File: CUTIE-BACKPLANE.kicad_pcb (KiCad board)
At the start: 2 copper layers, 6 parts, among them J1 ERF8-025-05.0-L-DV-L-K-TR, J2 ERF8-025-05.0-L-DV-L-K-TR, J3 ERF8-025-05.0-L-DV-L-K-TR, J4 ERF8-025-05.0-L-DV-L-K-TR, J5 ERF8-025-05.0-L-DV-L-K-TR, J6 ERF8-025-05.0-L-DV-L-K-TR

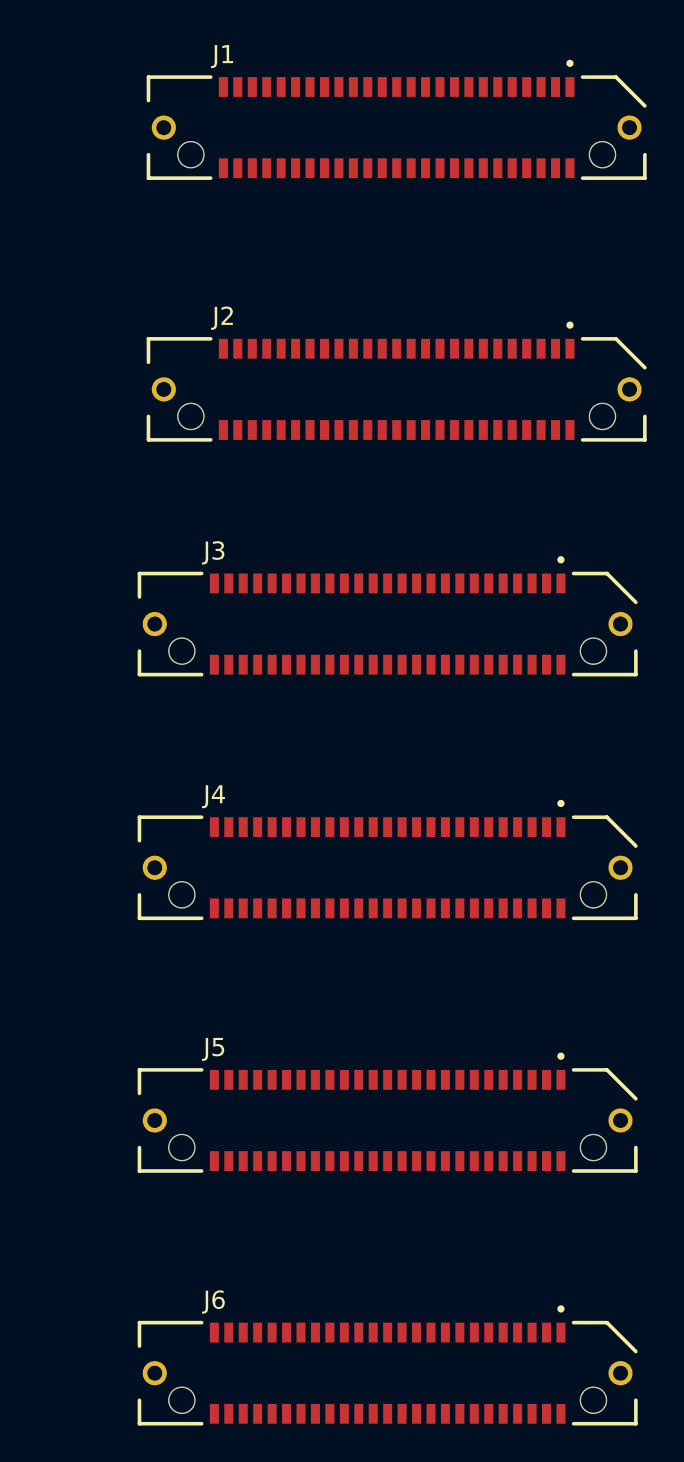
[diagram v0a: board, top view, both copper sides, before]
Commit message: fixed footprint link
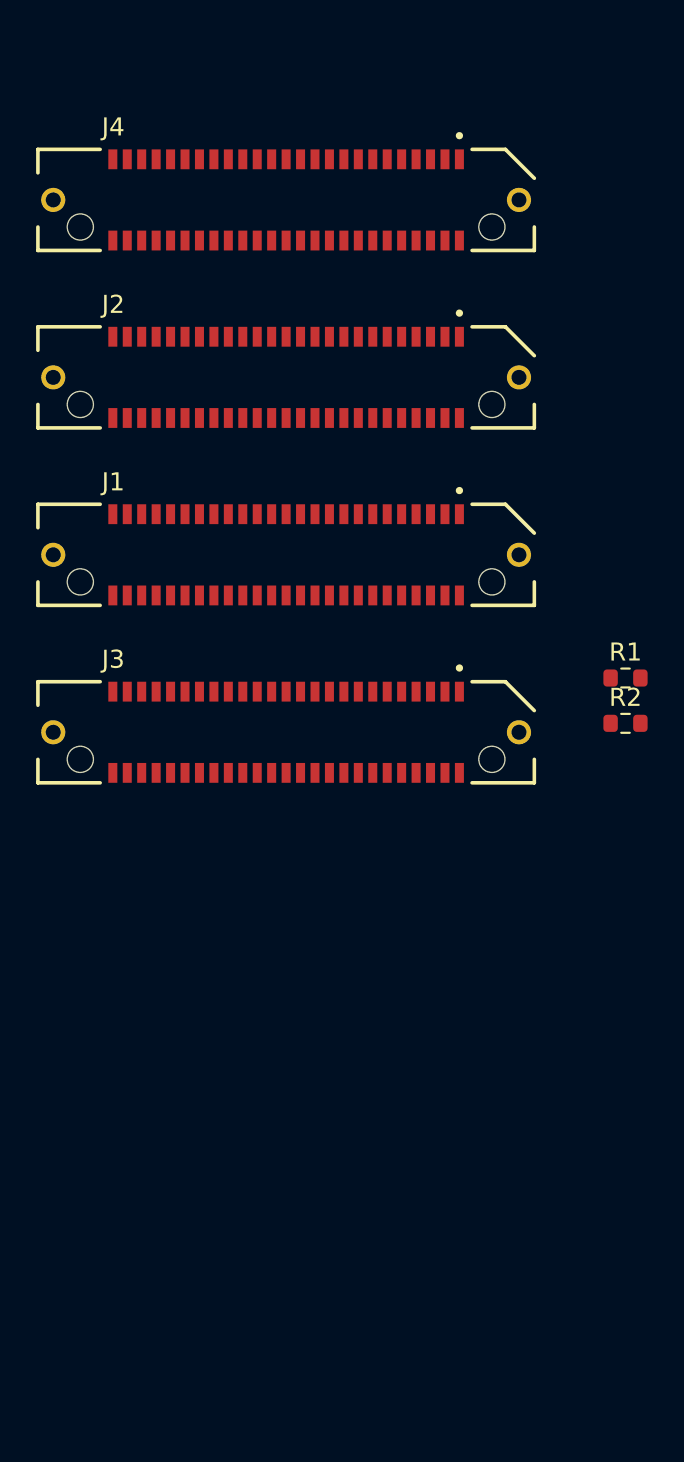
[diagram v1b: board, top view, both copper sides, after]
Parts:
- removed J5, J6: ERF8-025-05.0-L-DV-L-K-TR, library:SAMTEC_ERF8-025-05.0-L-DV-L-K-TR
- added R1: 120, Resistor_SMD:R_0603_1608Metric, F.Cu at (163.2, 95.0)
- added R2: 120, Resistor_SMD:R_0603_1608Metric, F.Cu at (163.2, 97.5)
- moved J4 37.4 mm to (144.4, 68.5)
- moved J1 24.4 mm to (144.4, 88.2)
- moved J3 8.22 mm to (144.4, 98.0)
- moved J2 6.16 mm to (144.4, 78.3)
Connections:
- J1 pad 01: (no net) -> /Slot 1/CAN0.L
- J1 pad 02: (no net) -> GND
- J1 pad 03: (no net) -> /Slot 1/CAN0.H
- J1 pad 04: (no net) -> GND
- J1 pad 05: (no net) -> GND
- J1 pad 06: (no net) -> unconnected-(J1-Pad06)
- J1 pad 07: (no net) -> GND
- J1 pad 08: (no net) -> unconnected-(J1-Pad08)
- J1 pad 09: (no net) -> unconnected-(J1-Pad09)
- J1 pad 10: unconnected-(J1-Pad10) -> GND
- J1 pad 12: unconnected-(J1-Pad12) -> GND
- J1 pad 13: unconnected-(J1-Pad13) -> GND
- J1 pad 15: unconnected-(J1-Pad15) -> GND
- J1 pad 18: unconnected-(J1-Pad18) -> GND
- J1 pad 20: unconnected-(J1-Pad20) -> GND
- J1 pad 21: unconnected-(J1-Pad21) -> GND
- J1 pad 22: unconnected-(J1-Pad22) -> GND
- J1 pad 23: unconnected-(J1-Pad23) -> GND
- J1 pad 24: unconnected-(J1-Pad24) -> GND
- J1 pad 25: unconnected-(J1-Pad25) -> GND
- J1 pad 26: unconnected-(J1-Pad26) -> GND
- J1 pad 27: unconnected-(J1-Pad27) -> GND
- J1 pad 28: unconnected-(J1-Pad28) -> GND
- J1 pad 29: unconnected-(J1-Pad29) -> GND
- J1 pad 30: unconnected-(J1-Pad30) -> GND
- J1 pad 31: unconnected-(J1-Pad31) -> /Slot 1/5V0_3
- J1 pad 32: unconnected-(J1-Pad32) -> /Slot 1/5V0_USB
- J1 pad 33: unconnected-(J1-Pad33) -> /Slot 1/5V0_3
- J1 pad 34: unconnected-(J1-Pad34) -> /Slot 1/5V0_USB
- J1 pad 35: unconnected-(J1-Pad35) -> /Slot 1/5V0_3
- J1 pad 36: unconnected-(J1-Pad36) -> /Slot 1/5V0_USB
- J1 pad 37: unconnected-(J1-Pad37) -> /Slot 1/5V0_3
- J1 pad 38: unconnected-(J1-Pad38) -> /Slot 1/5V0_USB
- J1 pad 39: unconnected-(J1-Pad39) -> /Slot 1/5V0_3
- J1 pad 40: unconnected-(J1-Pad40) -> /Slot 1/5V0_USB
- J1 pad 41: unconnected-(J1-Pad41) -> /Slot 1/5V0_1
- J1 pad 42: unconnected-(J1-Pad42) -> /Slot 1/5V0_2
- J1 pad 43: unconnected-(J1-Pad43) -> /Slot 1/5V0_1
- J1 pad 44: unconnected-(J1-Pad44) -> /Slot 1/5V0_2
- J1 pad 45: unconnected-(J1-Pad45) -> /Slot 1/5V0_1
- J1 pad 46: unconnected-(J1-Pad46) -> /Slot 1/5V0_2
- J1 pad 47: unconnected-(J1-Pad47) -> /Slot 1/5V0_1
- J1 pad 48: unconnected-(J1-Pad48) -> /Slot 1/5V0_2
- J1 pad 49: unconnected-(J1-Pad49) -> /Slot 1/5V0_1
- J1 pad 50: unconnected-(J1-Pad50) -> /Slot 1/5V0_2
- J2 pad 01: (no net) -> /Slot 1/CAN0.L
- J2 pad 02: (no net) -> GND
- J2 pad 03: (no net) -> /Slot 1/CAN0.H
- J2 pad 04: (no net) -> GND
- J2 pad 05: (no net) -> GND
- J2 pad 06: (no net) -> /Slot 2/USB3.D_N
- J2 pad 07: (no net) -> GND
- J2 pad 08: (no net) -> /Slot 2/USB3.D_P
- J2 pad 09: (no net) -> unconnected-(J2-Pad09)
- J2 pad 10: unconnected-(J2-Pad10) -> GND
- J2 pad 12: unconnected-(J2-Pad12) -> GND
- J2 pad 13: unconnected-(J2-Pad13) -> GND
- J2 pad 14: unconnected-(J2-Pad14) -> /Slot 2/USB3.RX_N
- J2 pad 15: unconnected-(J2-Pad15) -> GND
- J2 pad 16: unconnected-(J2-Pad16) -> /Slot 2/USB3.RX_P
- J2 pad 18: unconnected-(J2-Pad18) -> GND
- J2 pad 20: unconnected-(J2-Pad20) -> GND
- J2 pad 21: unconnected-(J2-Pad21) -> GND
- J2 pad 22: unconnected-(J2-Pad22) -> /Slot 2/USB3.TX_N
- J2 pad 23: unconnected-(J2-Pad23) -> GND
- J2 pad 24: unconnected-(J2-Pad24) -> /Slot 2/USB3.TX_P
- J2 pad 26: unconnected-(J2-Pad26) -> GND
- J2 pad 28: unconnected-(J2-Pad28) -> GND
- J2 pad 29: unconnected-(J2-Pad29) -> GND
- J2 pad 30: unconnected-(J2-Pad30) -> /Slot 2/CMRF.MOSI
- J2 pad 31: unconnected-(J2-Pad31) -> GND
- J2 pad 32: unconnected-(J2-Pad32) -> /Slot 2/CMRF.MISO
- J2 pad 34: unconnected-(J2-Pad34) -> GND
- J2 pad 36: unconnected-(J2-Pad36) -> GND
- J2 pad 37: unconnected-(J2-Pad37) -> GND
- J2 pad 38: unconnected-(J2-Pad38) -> /Slot 2/CMRF.SCLK
- J2 pad 39: unconnected-(J2-Pad39) -> GND
- J2 pad 40: unconnected-(J2-Pad40) -> /Slot 2/CMRF.CS0n
- J2 pad 41: unconnected-(J2-Pad41) -> /Slot 1/5V0_1
- J2 pad 42: unconnected-(J2-Pad42) -> GND
- J2 pad 43: unconnected-(J2-Pad43) -> /Slot 1/5V0_1
- J2 pad 44: unconnected-(J2-Pad44) -> GND
- J2 pad 45: unconnected-(J2-Pad45) -> /Slot 1/5V0_1
- J2 pad 47: unconnected-(J2-Pad47) -> /Slot 1/5V0_1
- J2 pad 49: unconnected-(J2-Pad49) -> /Slot 1/5V0_1
- J2 pad 50: unconnected-(J2-Pad50) -> GND
- J3 pad 01: (no net) -> /Slot 1/CAN0.L
- J3 pad 02: (no net) -> GND
- J3 pad 03: (no net) -> /Slot 1/CAN0.H
- J3 pad 04: (no net) -> GND
- J3 pad 05: (no net) -> GND
- J3 pad 06: (no net) -> unconnected-(J3-Pad06)
- J3 pad 07: (no net) -> GND
- J3 pad 08: (no net) -> unconnected-(J3-Pad08)
- J3 pad 09: (no net) -> unconnected-(J3-Pad09)
- J3 pad 10: unconnected-(J3-Pad10) -> GND
- J3 pad 12: unconnected-(J3-Pad12) -> GND
- J3 pad 13: unconnected-(J3-Pad13) -> GND
- J3 pad 15: unconnected-(J3-Pad15) -> GND
- J3 pad 18: unconnected-(J3-Pad18) -> GND
- J3 pad 20: unconnected-(J3-Pad20) -> GND
- J3 pad 21: unconnected-(J3-Pad21) -> GND
- J3 pad 23: unconnected-(J3-Pad23) -> GND
- J3 pad 26: unconnected-(J3-Pad26) -> GND
- J3 pad 28: unconnected-(J3-Pad28) -> GND
- J3 pad 29: unconnected-(J3-Pad29) -> GND
- J3 pad 31: unconnected-(J3-Pad31) -> GND
- J3 pad 34: unconnected-(J3-Pad34) -> GND
- J3 pad 36: unconnected-(J3-Pad36) -> GND
- J3 pad 37: unconnected-(J3-Pad37) -> GND
- J3 pad 39: unconnected-(J3-Pad39) -> GND
- J3 pad 41: unconnected-(J3-Pad41) -> /Slot 1/5V0_2
- J3 pad 42: unconnected-(J3-Pad42) -> GND
- J3 pad 43: unconnected-(J3-Pad43) -> /Slot 1/5V0_2
- J3 pad 44: unconnected-(J3-Pad44) -> GND
- J3 pad 45: unconnected-(J3-Pad45) -> /Slot 1/5V0_2
- J3 pad 47: unconnected-(J3-Pad47) -> /Slot 1/5V0_2
- J3 pad 49: unconnected-(J3-Pad49) -> /Slot 1/5V0_2
- J3 pad 50: unconnected-(J3-Pad50) -> GND
- J4 pad 01: (no net) -> /Slot 1/CAN0.L
- J4 pad 02: (no net) -> GND
- J4 pad 03: (no net) -> /Slot 1/CAN0.H
- J4 pad 04: (no net) -> GND
- J4 pad 05: (no net) -> GND
- J4 pad 06: (no net) -> unconnected-(J4-Pad06)
- J4 pad 07: (no net) -> GND
- J4 pad 08: (no net) -> unconnected-(J4-Pad08)
- J4 pad 09: (no net) -> unconnected-(J4-Pad09)
- J4 pad 10: unconnected-(J4-Pad10) -> GND
- J4 pad 12: unconnected-(J4-Pad12) -> GND
- J4 pad 13: unconnected-(J4-Pad13) -> GND
- J4 pad 15: unconnected-(J4-Pad15) -> GND
- J4 pad 18: unconnected-(J4-Pad18) -> GND
- J4 pad 20: unconnected-(J4-Pad20) -> GND
- J4 pad 21: unconnected-(J4-Pad21) -> GND
- J4 pad 23: unconnected-(J4-Pad23) -> GND
- J4 pad 26: unconnected-(J4-Pad26) -> GND
- J4 pad 28: unconnected-(J4-Pad28) -> GND
- J4 pad 29: unconnected-(J4-Pad29) -> GND
- J4 pad 30: unconnected-(J4-Pad30) -> /Slot 2/CMRF.MOSI
- J4 pad 31: unconnected-(J4-Pad31) -> GND
- J4 pad 32: unconnected-(J4-Pad32) -> /Slot 2/CMRF.MISO
- J4 pad 34: unconnected-(J4-Pad34) -> GND
- J4 pad 36: unconnected-(J4-Pad36) -> GND
- J4 pad 37: unconnected-(J4-Pad37) -> GND
- J4 pad 38: unconnected-(J4-Pad38) -> /Slot 2/CMRF.SCLK
- J4 pad 39: unconnected-(J4-Pad39) -> GND
- J4 pad 40: unconnected-(J4-Pad40) -> /Slot 2/CMRF.CS0n
- J4 pad 41: unconnected-(J4-Pad41) -> /Slot 1/5V0_3
- J4 pad 42: unconnected-(J4-Pad42) -> GND
- J4 pad 43: unconnected-(J4-Pad43) -> /Slot 1/5V0_3
- J4 pad 44: unconnected-(J4-Pad44) -> GND
- J4 pad 45: unconnected-(J4-Pad45) -> /Slot 1/5V0_3
- J4 pad 47: unconnected-(J4-Pad47) -> /Slot 1/5V0_3
- J4 pad 49: unconnected-(J4-Pad49) -> /Slot 1/5V0_3
- J4 pad 50: unconnected-(J4-Pad50) -> GND

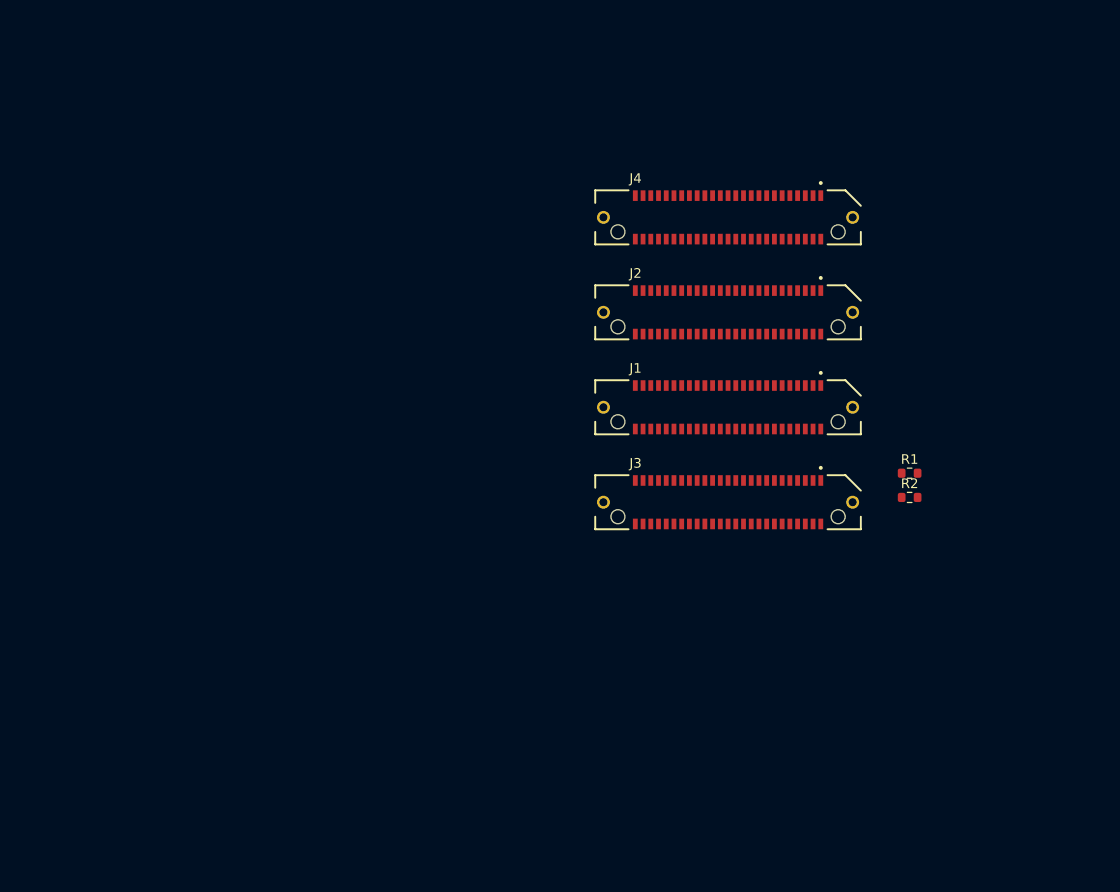
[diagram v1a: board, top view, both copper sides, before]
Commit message: added pwr leds and edge cuts
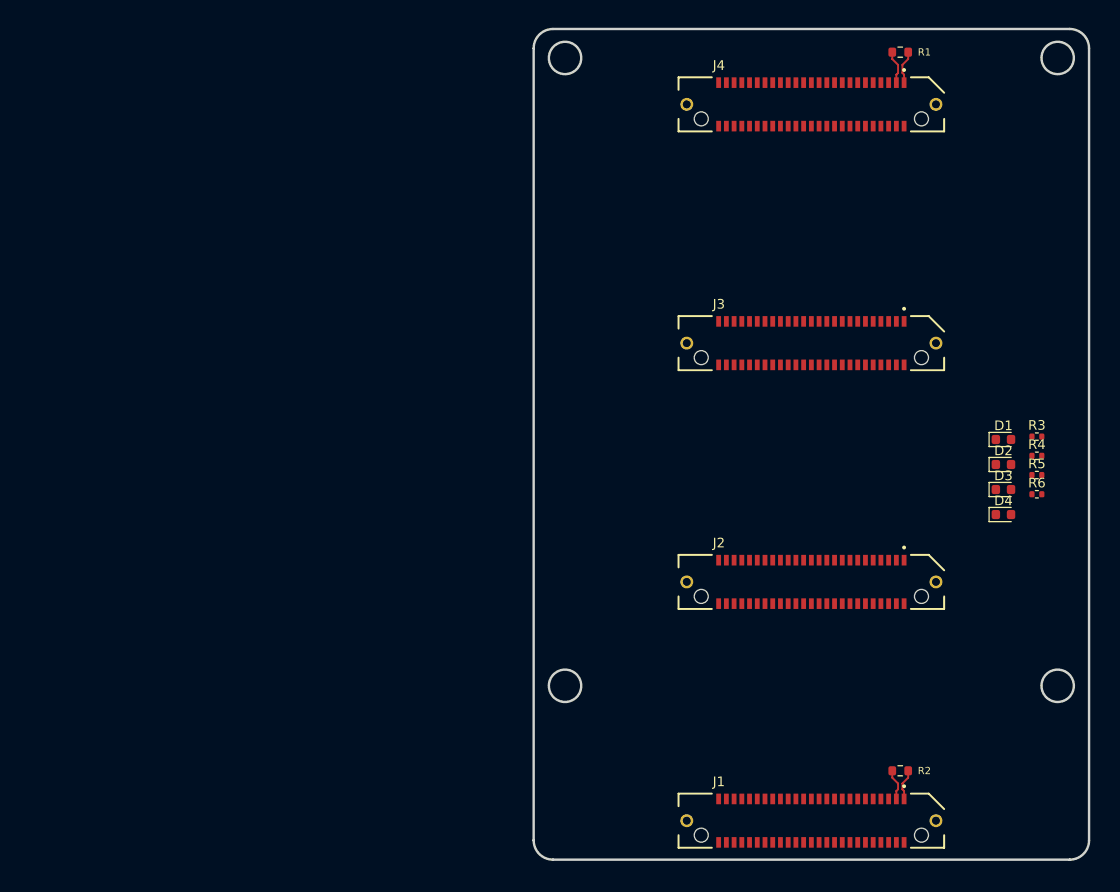
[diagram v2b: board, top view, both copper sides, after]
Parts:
- added D1: LED Red, LED_SMD:LED_0603_1608Metric, F.Cu at (172.9, 91.5)
- added D2: LED Red, LED_SMD:LED_0603_1608Metric, F.Cu at (172.9, 94.1)
- added D3: LED Red, LED_SMD:LED_0603_1608Metric, F.Cu at (172.9, 96.7)
- added D4: LED Red, LED_SMD:LED_0603_1608Metric, F.Cu at (172.9, 99.3)
- added R3: 1k, Resistor_SMD:R_0402_1005Metric, F.Cu at (176.3, 91.2)
- added R4: 1k, Resistor_SMD:R_0402_1005Metric, F.Cu at (176.3, 93.2)
- added R5: 1k, Resistor_SMD:R_0402_1005Metric, F.Cu at (176.3, 95.2)
- added R6: 1k, Resistor_SMD:R_0402_1005Metric, F.Cu at (176.3, 97.2)
- moved J1 43.7 mm to (153.0, 131.0)
- moved R1 43.6 mm to (162.2, 51.4)
- moved J2 29.2 mm to (153.0, 106.2)
- moved R2 28.3 mm to (162.2, 125.8)
- moved J3 18.6 mm to (153.0, 81.5)
- moved J4 14.5 mm to (153.0, 56.8)
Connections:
- net /Slot 1/CAN0.H renamed /Slot 1/CAN0.P
- net /Slot 1/CAN0.L renamed /Slot 1/CAN0.N
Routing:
- net /Slot 1/CAN0.P: track 0.00 -> 6.71 mm
- net /Slot 1/CAN0.N: track 0.00 -> 6.71 mm
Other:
- board outline added: 57.5 x 86 mm

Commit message: prelim layout complete
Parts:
- added J7: USB3_A, library:CONN9_08-0003_MOL, F.Cu at (156.0, 94.0)
- moved R5 57.1 mm to (134.8, 56.0)
- moved D3 56.8 mm to (134.8, 54.5)
- moved R3 43.9 mm to (134.8, 105.4)
- moved R4 43.4 mm to (134.8, 80.7)
- moved D2 40.9 mm to (134.8, 79.2)
- moved D1 40.1 mm to (134.8, 103.9)
- moved R6 34.2 mm to (142.2, 95.5)
- moved D4 31.1 mm to (142.2, 94.0)
- moved R2 22.0 mm to (140.2, 126.8), turned to 180 degrees
- moved R1 21.2 mm to (143.8, 62.0), turned to 180 degrees
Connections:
- J1 pad 01: /Slot 1/CAN0.N -> /Slot 1/5V0_2
- J1 pad 02: GND -> /Slot 1/5V0_1
- J1 pad 03: /Slot 1/CAN0.P -> /Slot 1/5V0_2
- J1 pad 04: GND -> /Slot 1/5V0_1
- J1 pad 05: GND -> /Slot 1/5V0_2
- J1 pad 06: unconnected-(J1-Pad06) -> /Slot 1/5V0_1
- J1 pad 07: GND -> /Slot 1/5V0_2
- J1 pad 08: unconnected-(J1-Pad08) -> /Slot 1/5V0_1
- J1 pad 09: unconnected-(J1-Pad09) -> /Slot 1/5V0_2
- J1 pad 10: GND -> /Slot 1/5V0_1
- J1 pad 11: unconnected-(J1-Pad11) -> /Slot 1/5V0_USB
- J1 pad 12: GND -> /Slot 1/5V0_3
- J1 pad 13: GND -> /Slot 1/5V0_USB
- J1 pad 14: unconnected-(J1-Pad14) -> /Slot 1/5V0_3
- J1 pad 15: GND -> /Slot 1/5V0_USB
- J1 pad 16: unconnected-(J1-Pad16) -> /Slot 1/5V0_3
- J1 pad 17: unconnected-(J1-Pad17) -> /Slot 1/5V0_USB
- J1 pad 18: GND -> /Slot 1/5V0_3
- J1 pad 19: unconnected-(J1-Pad19) -> /Slot 1/5V0_USB
- J1 pad 20: GND -> /Slot 1/5V0_3
- J1 pad 31: /Slot 1/5V0_3 -> GND
- J1 pad 32: /Slot 1/5V0_USB -> unconnected-(J1-Pad32)
- J1 pad 33: /Slot 1/5V0_3 -> GND
- J1 pad 34: /Slot 1/5V0_USB -> unconnected-(J1-Pad34)
- J1 pad 35: /Slot 1/5V0_3 -> unconnected-(J1-Pad35)
- J1 pad 36: /Slot 1/5V0_USB -> GND
- J1 pad 37: /Slot 1/5V0_3 -> unconnected-(J1-Pad37)
- J1 pad 38: /Slot 1/5V0_USB -> GND
- J1 pad 39: /Slot 1/5V0_3 -> GND
- J1 pad 40: /Slot 1/5V0_USB -> unconnected-(J1-Pad40)
- J1 pad 41: /Slot 1/5V0_1 -> GND
- J1 pad 42: /Slot 1/5V0_2 -> unconnected-(J1-Pad42)
- J1 pad 43: /Slot 1/5V0_1 -> unconnected-(J1-Pad43)
- J1 pad 44: /Slot 1/5V0_2 -> GND
- J1 pad 45: /Slot 1/5V0_1 -> unconnected-(J1-Pad45)
- J1 pad 46: /Slot 1/5V0_2 -> GND
- J1 pad 47: /Slot 1/5V0_1 -> GND
- J1 pad 48: /Slot 1/5V0_2 -> /Slot 1/CAN0.P
- J1 pad 49: /Slot 1/5V0_1 -> GND
- J1 pad 50: /Slot 1/5V0_2 -> /Slot 1/CAN0.N
- J2 pad 01: /Slot 1/CAN0.N -> GND
- J2 pad 02: GND -> /Slot 1/5V0_1
- J2 pad 03: /Slot 1/CAN0.P -> unconnected-(J2-Pad03)
- J2 pad 04: GND -> /Slot 1/5V0_1
- J2 pad 05: GND -> unconnected-(J2-Pad05)
- J2 pad 06: /Slot 2/USB3.D_N -> /Slot 1/5V0_1
- J2 pad 08: /Slot 2/USB3.D_P -> /Slot 1/5V0_1
- J2 pad 09: unconnected-(J2-Pad09) -> GND
- J2 pad 10: GND -> /Slot 1/5V0_1
- J2 pad 11: unconnected-(J2-Pad11) -> /Slot 2/CMRF.CS0n
- J2 pad 13: GND -> /Slot 2/CMRF.SCLK
- J2 pad 14: /Slot 2/USB3.RX_N -> GND
- J2 pad 16: /Slot 2/USB3.RX_P -> unconnected-(J2-Pad16)
- J2 pad 17: unconnected-(J2-Pad17) -> GND
- J2 pad 18: GND -> unconnected-(J2-Pad18)
- J2 pad 19: unconnected-(J2-Pad19) -> /Slot 2/CMRF.MISO
- J2 pad 21: GND -> /Slot 2/CMRF.MOSI
- J2 pad 22: /Slot 2/USB3.TX_N -> GND
- J2 pad 24: /Slot 2/USB3.TX_P -> unconnected-(J2-Pad24)
- J2 pad 25: unconnected-(J2-Pad25) -> GND
- J2 pad 26: GND -> unconnected-(J2-Pad26)
- J2 pad 27: unconnected-(J2-Pad27) -> /Slot 2/USB3.TX_P
- J2 pad 29: GND -> /Slot 2/USB3.TX_N
- J2 pad 30: /Slot 2/CMRF.MOSI -> GND
- J2 pad 32: /Slot 2/CMRF.MISO -> unconnected-(J2-Pad32)
- J2 pad 33: unconnected-(J2-Pad33) -> GND
- J2 pad 34: GND -> unconnected-(J2-Pad34)
- J2 pad 35: unconnected-(J2-Pad35) -> /Slot 2/USB3.RX_P
- J2 pad 37: GND -> /Slot 2/USB3.RX_N
- J2 pad 38: /Slot 2/CMRF.SCLK -> GND
- J2 pad 40: /Slot 2/CMRF.CS0n -> unconnected-(J2-Pad40)
- J2 pad 41: /Slot 1/5V0_1 -> GND
- J2 pad 42: GND -> unconnected-(J2-Pad42)
- J2 pad 43: /Slot 1/5V0_1 -> /Slot 2/USB3.D_P
- J2 pad 45: /Slot 1/5V0_1 -> /Slot 2/USB3.D_N
- J2 pad 46: unconnected-(J2-Pad46) -> GND
- J2 pad 47: /Slot 1/5V0_1 -> GND
- J2 pad 48: unconnected-(J2-Pad48) -> /Slot 1/CAN0.P
- J2 pad 49: /Slot 1/5V0_1 -> GND
- J2 pad 50: GND -> /Slot 1/CAN0.N
- J3 pad 01: /Slot 1/CAN0.N -> GND
- J3 pad 02: GND -> /Slot 1/5V0_2
- J3 pad 03: /Slot 1/CAN0.P -> unconnected-(J3-Pad03)
- J3 pad 04: GND -> /Slot 1/5V0_2
- J3 pad 05: GND -> unconnected-(J3-Pad05)
- J3 pad 06: unconnected-(J3-Pad06) -> /Slot 1/5V0_2
- J3 pad 08: unconnected-(J3-Pad08) -> /Slot 1/5V0_2
- J3 pad 09: unconnected-(J3-Pad09) -> GND
- J3 pad 10: GND -> /Slot 1/5V0_2
- J3 pad 13: GND -> unconnected-(J3-Pad13)
- J3 pad 14: unconnected-(J3-Pad14) -> GND
- J3 pad 17: unconnected-(J3-Pad17) -> GND
- J3 pad 18: GND -> unconnected-(J3-Pad18)
- J3 pad 21: GND -> unconnected-(J3-Pad21)
- J3 pad 22: unconnected-(J3-Pad22) -> GND
- J3 pad 25: unconnected-(J3-Pad25) -> GND
- J3 pad 26: GND -> unconnected-(J3-Pad26)
- J3 pad 29: GND -> unconnected-(J3-Pad29)
- J3 pad 30: unconnected-(J3-Pad30) -> GND
- J3 pad 33: unconnected-(J3-Pad33) -> GND
- J3 pad 34: GND -> unconnected-(J3-Pad34)
- J3 pad 37: GND -> unconnected-(J3-Pad37)
- J3 pad 38: unconnected-(J3-Pad38) -> GND
- J3 pad 41: /Slot 1/5V0_2 -> GND
- J3 pad 42: GND -> unconnected-(J3-Pad42)
- J3 pad 43: /Slot 1/5V0_2 -> unconnected-(J3-Pad43)
- J3 pad 45: /Slot 1/5V0_2 -> unconnected-(J3-Pad45)
- J3 pad 46: unconnected-(J3-Pad46) -> GND
- J3 pad 47: /Slot 1/5V0_2 -> GND
- J3 pad 48: unconnected-(J3-Pad48) -> /Slot 1/CAN0.P
- J3 pad 49: /Slot 1/5V0_2 -> GND
- J3 pad 50: GND -> /Slot 1/CAN0.N
- J4 pad 01: /Slot 1/CAN0.N -> GND
- J4 pad 02: GND -> /Slot 1/5V0_3
- J4 pad 03: /Slot 1/CAN0.P -> unconnected-(J4-Pad03)
- J4 pad 04: GND -> /Slot 1/5V0_3
- J4 pad 05: GND -> unconnected-(J4-Pad05)
- J4 pad 06: unconnected-(J4-Pad06) -> /Slot 1/5V0_3
- J4 pad 08: unconnected-(J4-Pad08) -> /Slot 1/5V0_3
- J4 pad 09: unconnected-(J4-Pad09) -> GND
- J4 pad 10: GND -> /Slot 1/5V0_3
- J4 pad 11: unconnected-(J4-Pad11) -> /Slot 2/CMRF.CS0n
- J4 pad 13: GND -> /Slot 2/CMRF.SCLK
- J4 pad 14: unconnected-(J4-Pad14) -> GND
- J4 pad 17: unconnected-(J4-Pad17) -> GND
- J4 pad 18: GND -> unconnected-(J4-Pad18)
- J4 pad 19: unconnected-(J4-Pad19) -> /Slot 2/CMRF.MISO
- J4 pad 21: GND -> /Slot 2/CMRF.MOSI
- J4 pad 22: unconnected-(J4-Pad22) -> GND
- J4 pad 25: unconnected-(J4-Pad25) -> GND
- J4 pad 26: GND -> unconnected-(J4-Pad26)
- J4 pad 29: GND -> unconnected-(J4-Pad29)
- J4 pad 30: /Slot 2/CMRF.MOSI -> GND
- J4 pad 32: /Slot 2/CMRF.MISO -> unconnected-(J4-Pad32)
- J4 pad 33: unconnected-(J4-Pad33) -> GND
- J4 pad 34: GND -> unconnected-(J4-Pad34)
- J4 pad 37: GND -> unconnected-(J4-Pad37)
- J4 pad 38: /Slot 2/CMRF.SCLK -> GND
- J4 pad 40: /Slot 2/CMRF.CS0n -> unconnected-(J4-Pad40)
- J4 pad 41: /Slot 1/5V0_3 -> GND
- J4 pad 42: GND -> unconnected-(J4-Pad42)
- J4 pad 43: /Slot 1/5V0_3 -> unconnected-(J4-Pad43)
- J4 pad 45: /Slot 1/5V0_3 -> unconnected-(J4-Pad45)
- J4 pad 46: unconnected-(J4-Pad46) -> GND
- J4 pad 47: /Slot 1/5V0_3 -> GND
- J4 pad 48: unconnected-(J4-Pad48) -> /Slot 1/CAN0.P
- J4 pad 49: /Slot 1/5V0_3 -> GND
- J4 pad 50: GND -> /Slot 1/CAN0.N
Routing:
- net GND: track 0.00 -> 120.1 mm, vias 0 -> 93
- net /Slot 2/CMRF.MOSI: track 0.00 -> 89.5 mm, vias 0 -> 2
- net /Slot 2/CMRF.MISO: track 0.00 -> 84.9 mm, vias 0 -> 2
- net /Slot 2/CMRF.SCLK: track 0.00 -> 78.3 mm, vias 0 -> 2
- net /Slot 1/CAN0.P: track 6.71 -> 84.0 mm
- net /Slot 1/CAN0.N: track 6.71 -> 84.0 mm
- net /Slot 2/CMRF.CS0n: track 0.00 -> 73.7 mm
- net /Slot 1/5V0_1: track 0.00 -> 26.4 mm, vias 0 -> 15
- net /Slot 1/5V0_2: track 0.00 -> 26.4 mm, vias 0 -> 15
- net /Slot 1/5V0_3: track 0.00 -> 26.4 mm, vias 0 -> 15
- net /Slot 2/USB3.D_N: track 0.00 -> 19.1 mm
- net /Slot 2/USB3.D_P: track 0.00 -> 19.1 mm
- net /Slot 2/USB3.RX_P: track 0.00 -> 19.0 mm
- net /Slot 2/USB3.RX_N: track 0.00 -> 19.0 mm
- net /Slot 2/USB3.TX_P: track 0.00 -> 19.0 mm
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- added copper zone on F.Cu, net /Slot 1/5V0_1
- added copper zone on In2.Cu, net /Slot 1/5V0_1
- added copper zone on F.Cu, net /Slot 1/5V0_2
- added copper zone on In2.Cu, net /Slot 1/5V0_2
- added copper zone on F.Cu, net /Slot 1/5V0_3
- added copper zone on In2.Cu, net /Slot 1/5V0_3
- added copper zone on F.Cu, net /Slot 1/5V0_USB
- added copper zone on In2.Cu, net /Slot 1/5V0_USB
- added copper zone on B.Cu, net GND
- added copper zone on F.Cu, net GND
- added copper zone on In1.Cu, net GND
- added copper zone on In2.Cu, net GND
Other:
- copper layers 2 -> 4
- board text added: "SLOT 1"
- board text added: "SLOT 2"
- board text added: "SLOT 3"
- board text added: "SLOT 4"
- board text added: "WIFI"
